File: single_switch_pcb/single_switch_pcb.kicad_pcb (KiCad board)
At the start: 2 copper layers, 6 parts, among them J1 Conn_01x01_Female, J2 Conn_01x01_Female, J3 Conn_01x01_Female, J4 Conn_01x01_Female, U1 switchsocket

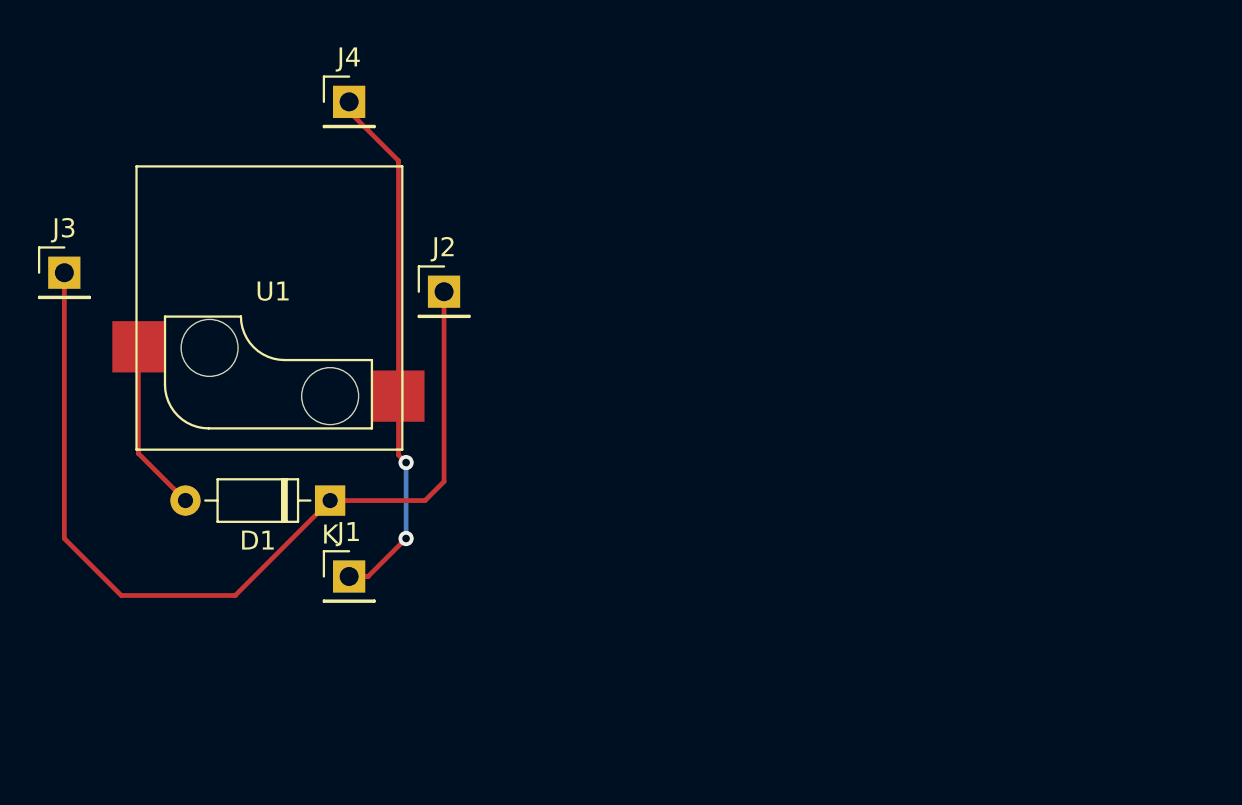
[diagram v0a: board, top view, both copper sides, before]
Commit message: finished routing. need to put M3 mounting holes on each corner then do checks if design is indeed compatible
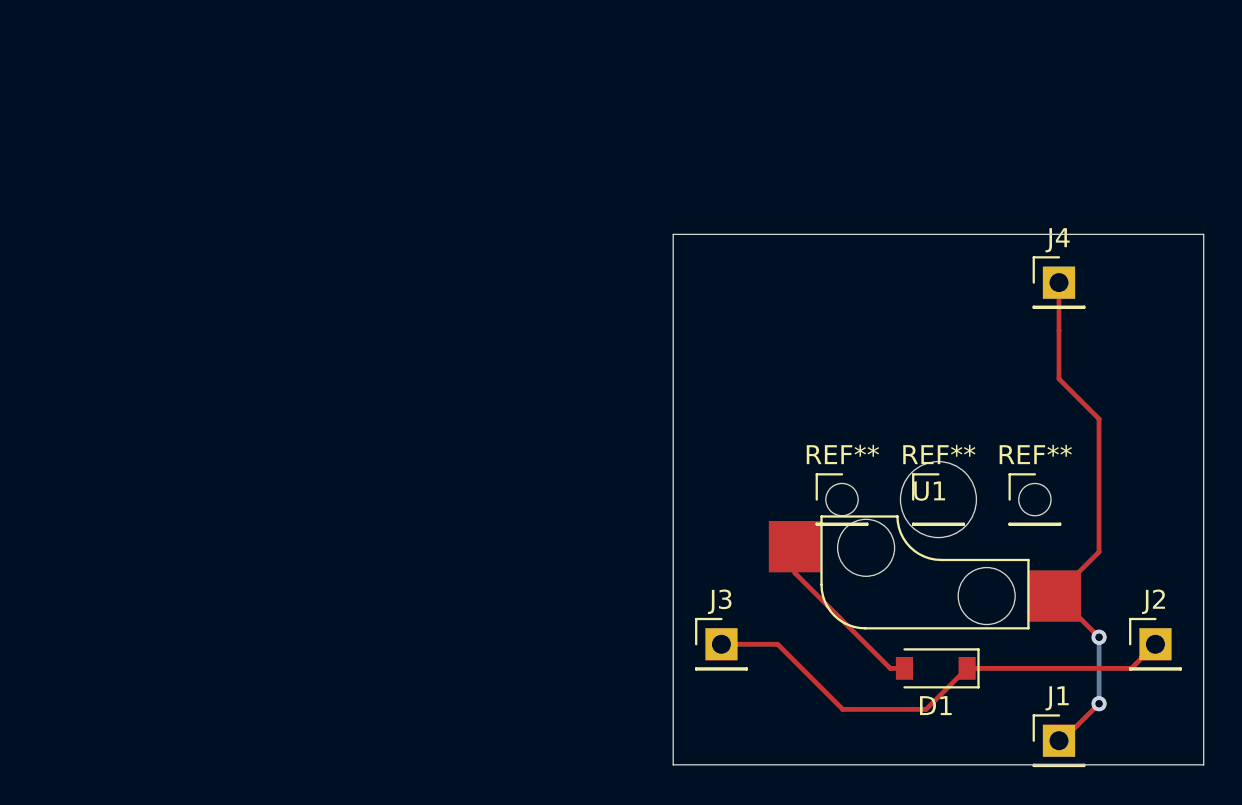
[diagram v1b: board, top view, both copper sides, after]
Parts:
- added REF**: PinHeader_1x01_P2.54mm_Vertical, Connector_PinHeader_2.54mm:PinHeader_1x01_P2.54mm_Vertical, F.Cu at (188.0, 108.0)
- added REF**: PinHeader_1x01_P2.54mm_Vertical, Connector_PinHeader_2.54mm:PinHeader_1x01_P2.54mm_Vertical, F.Cu at (198.1, 108.0)
- added REF**: PinHeader_1x01_P2.54mm_Vertical, Connector_PinHeader_2.54mm:PinHeader_1x01_P2.54mm_Vertical, F.Cu at (193.0, 108.0)
- D1: footprint Diode_THT:D_DO-35_SOD27_P7.62mm_Horizontal -> Diode_SMD:D_SOD-123
- moved J2 41.8 mm to (204.5, 115.6)
- moved J3 39.8 mm to (181.6, 115.6)
- moved J4 38.6 mm to (199.4, 96.5)
- moved J1 38.4 mm to (199.4, 120.7)
- moved U1 36.1 mm to (192.6, 112.5)
- moved D1 33.1 mm to (192.9, 116.8)
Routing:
- net Net-(D1-Pad1): track 47.7 -> 25.7 mm
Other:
- board outline added: 27.9 x 27.9 mm

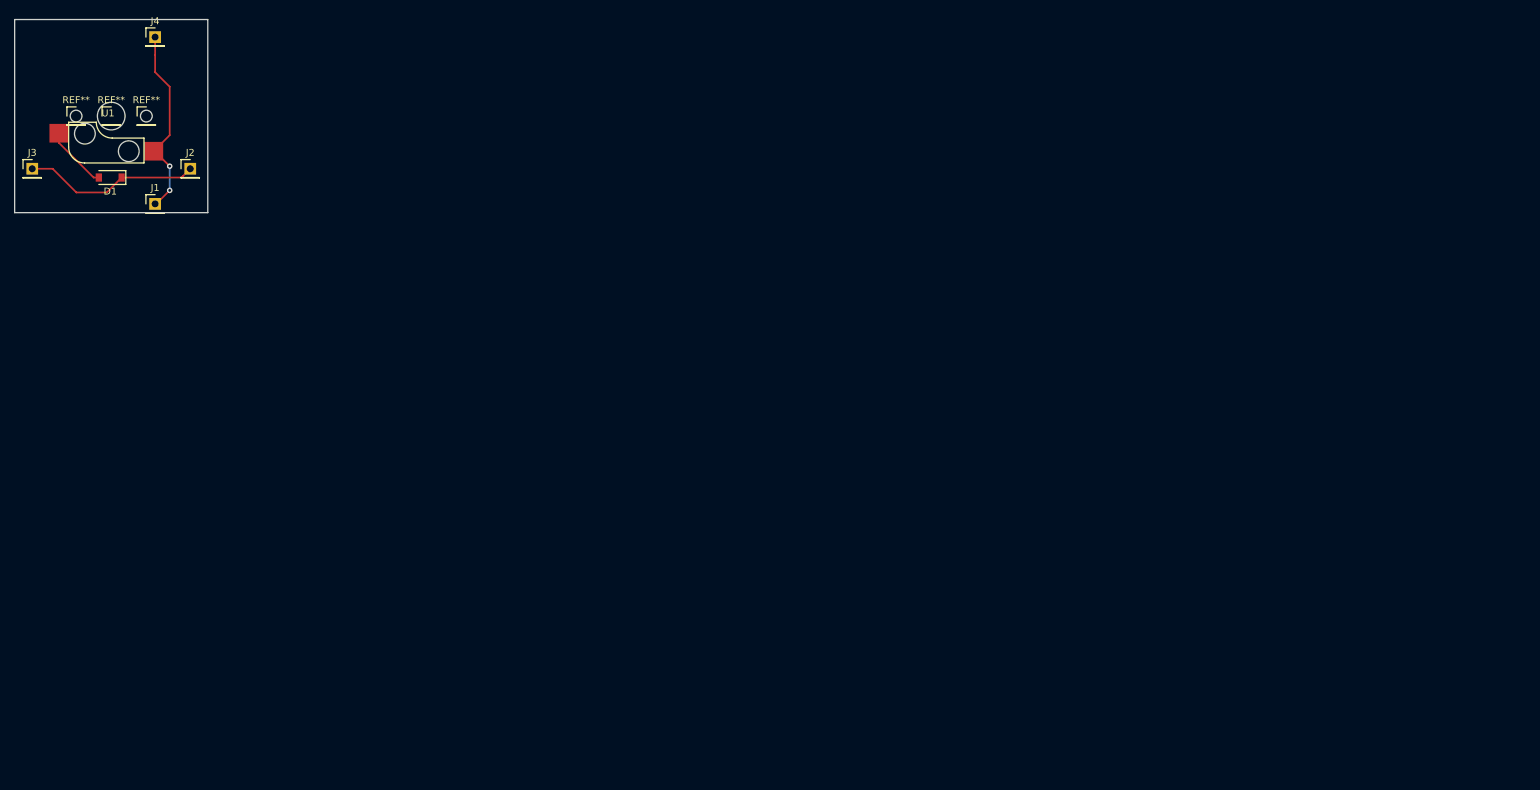
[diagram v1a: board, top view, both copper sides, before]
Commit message: finished pcb with M3 mounting. cleaned silkscreen. Need to print and test compatibility
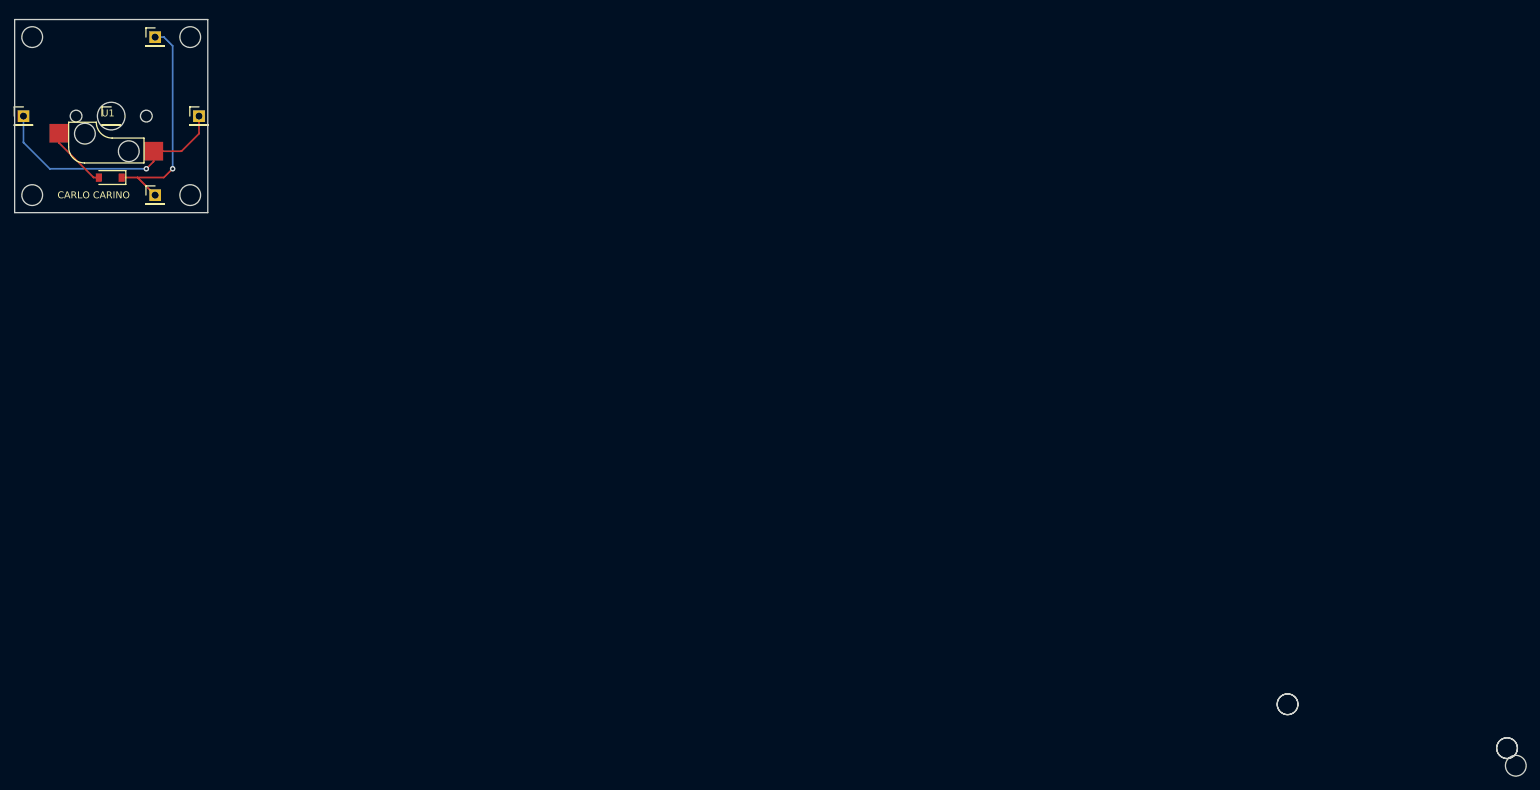
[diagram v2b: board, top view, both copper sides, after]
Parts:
- added ?: , , F.Cu at (214.6, 105.4)
- added ? (x2): , , F.Cu at (213.4, 102.9)
- added ? (x2): , , F.Cu at (181.6, 96.5)
- added REF**: M3hole, hotswapsocket:M3hole, F.Cu at (204.5, 96.5)
- added REF**: M3hole, hotswapsocket:M3hole, F.Cu at (181.6, 119.4)
- added REF**: PinHeader_1x01_P2.54mm_Vertical, Connector_PinHeader_2.54mm:PinHeader_1x01_P2.54mm_Vertical, F.Cu at (204.5, 119.4)
- added REF**: PinHeader_1x01_P2.54mm_Vertical, Connector_PinHeader_2.54mm:PinHeader_1x01_P2.54mm_Vertical, F.Cu at (181.6, 96.5)
- REF** (x2): value PinHeader_1x01_P2.54mm_Vertical -> hole1.7; footprint Connector_PinHeader_2.54mm:PinHeader_1x01_P2.54mm_Vertical -> hotswapsocket:hole1.7
- moved J1 22.9 mm to (180.3, 108.0)
- moved J2 19.7 mm to (199.4, 96.5)
- moved J3 18.2 mm to (199.4, 119.4)
- moved J4 13.1 mm to (205.7, 108.0)
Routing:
- net Net-(J1-Pad1): track 28.0 -> 36.4 mm, vias 2 -> 1
- net Net-(D1-Pad1): track 25.7 -> 32.3 mm, vias 0 -> 1
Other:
- board text added: "CARLO CARINO"

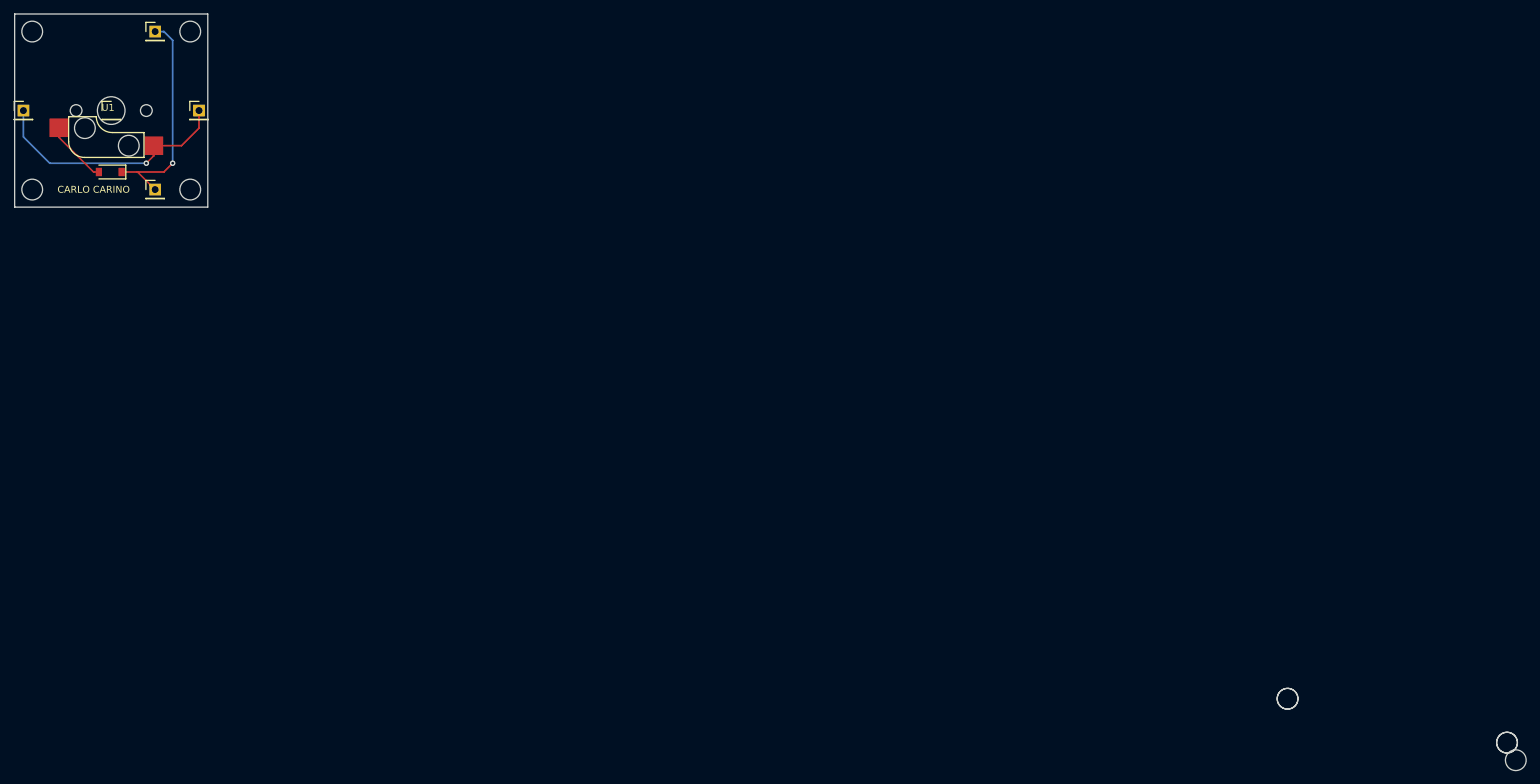
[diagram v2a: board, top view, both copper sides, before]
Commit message: edited pcb outline. needs smaller holes. created M2 and M1.6 holes
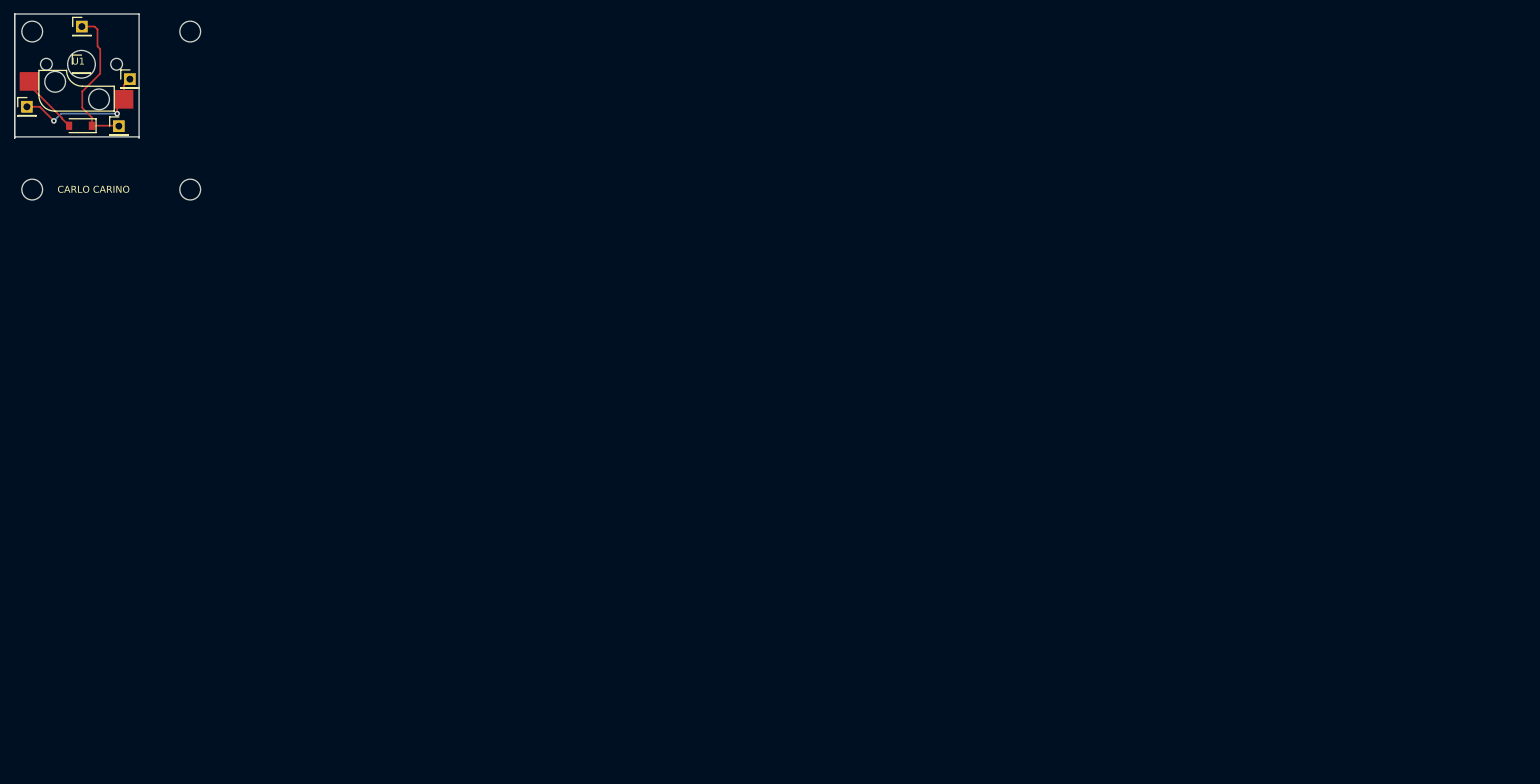
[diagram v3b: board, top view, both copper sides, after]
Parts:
- removed ? (x5): , 
- removed the REF** at (198.1, 108.0)
- removed the REF** at (188.0, 108.0)
- added REF**: hole1.7, hotswapsocket:hole1.7, F.Cu at (193.8, 101.2)
- added REF**: hole1.7, hotswapsocket:hole1.7, F.Cu at (183.7, 101.2)
- moved J4 11.0 mm to (195.8, 103.4)
- moved J2 10.6 mm to (188.8, 95.8)
- moved J3 10.6 mm to (194.2, 110.2)
- moved D1 7.96 mm to (188.6, 110.1)
- moved U1 7.96 mm to (188.3, 105.8)
- moved REF** 7.96 mm to (188.7, 101.2)
- moved J1 0.75 mm to (180.8, 107.4)
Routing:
- net Net-(J1-Pad1): track 36.4 -> 20.1 mm, vias 1 -> 2
- net Net-(D1-Pad1): track 32.3 -> 22.1 mm, vias 1 -> 0
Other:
- board size 27.9 x 27.9 mm -> 18 x 18 mm

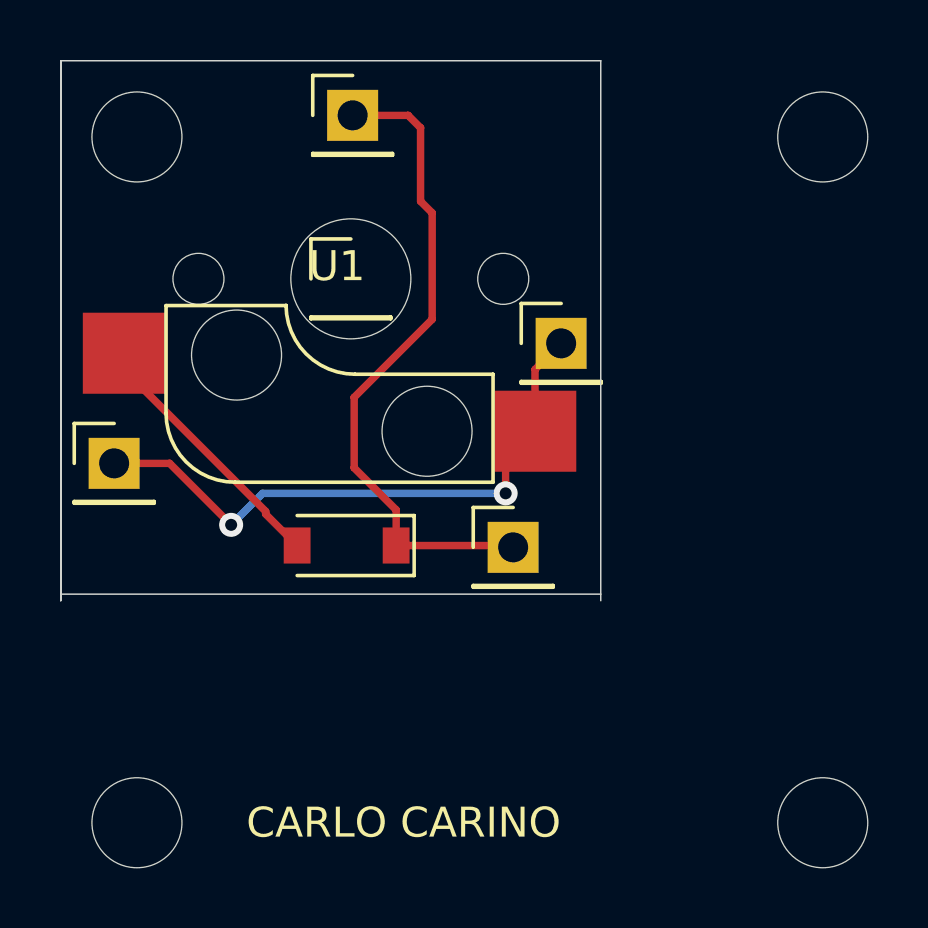
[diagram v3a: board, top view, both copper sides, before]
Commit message: m2 still big change to m1.6
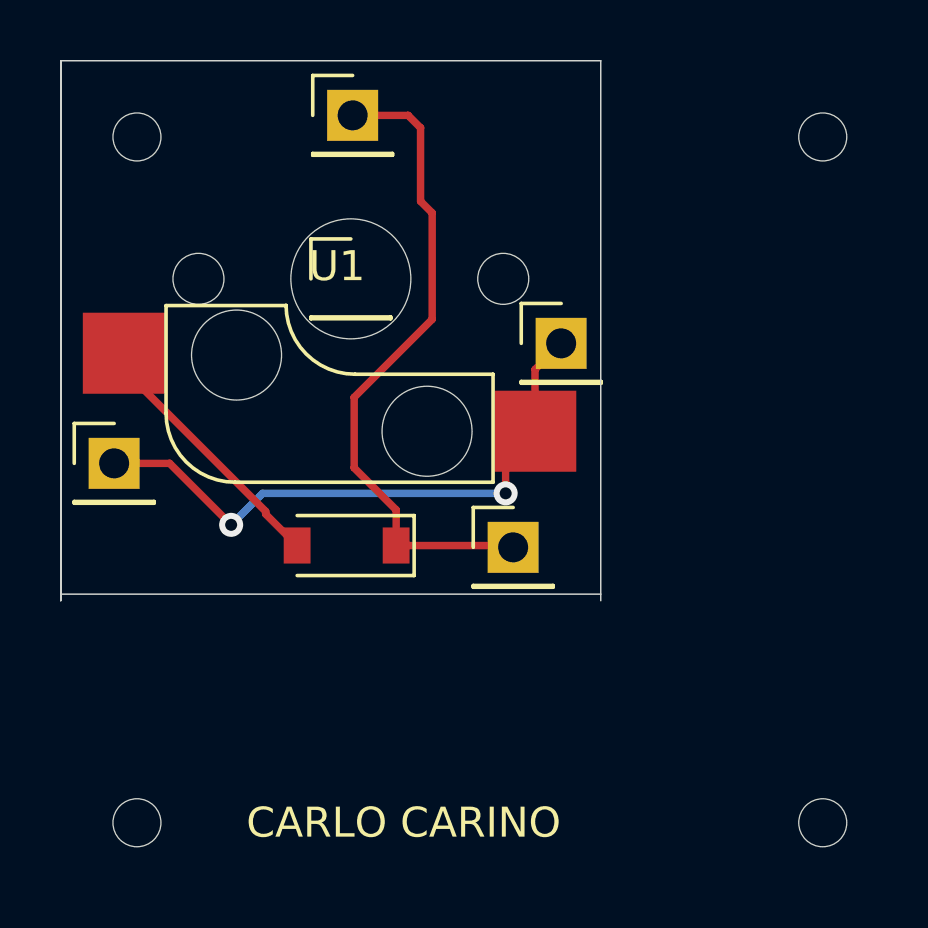
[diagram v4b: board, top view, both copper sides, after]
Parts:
- removed the REF** at (204.5, 96.5)
- removed the REF** at (181.6, 119.4)
- removed the REF** at (204.5, 119.4)
- removed the REF** at (181.6, 96.5)
- added REF**: m1.6hole, hotswapsocket:m1.6hole, F.Cu at (204.5, 96.5)
- added REF**: m1.6hole, hotswapsocket:m1.6hole, F.Cu at (204.5, 119.4)
- added REF**: m1.6hole, hotswapsocket:m1.6hole, F.Cu at (181.6, 119.4)
- added REF**: m1.6hole, hotswapsocket:m1.6hole, F.Cu at (181.6, 96.5)
